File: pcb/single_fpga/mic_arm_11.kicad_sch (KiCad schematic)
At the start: 17 parts, among them U110 CDCLVC1108PW, U89 IM72D128V01XTMA1, U90 IM72D128V01XTMA1, U91 IM72D128V01XTMA1, U92 IM72D128V01XTMA1, U93 IM72D128V01XTMA1, U94 IM72D128V01XTMA1, U95 IM72D128V01XTMA1, U96 IM72D128V01XTMA1

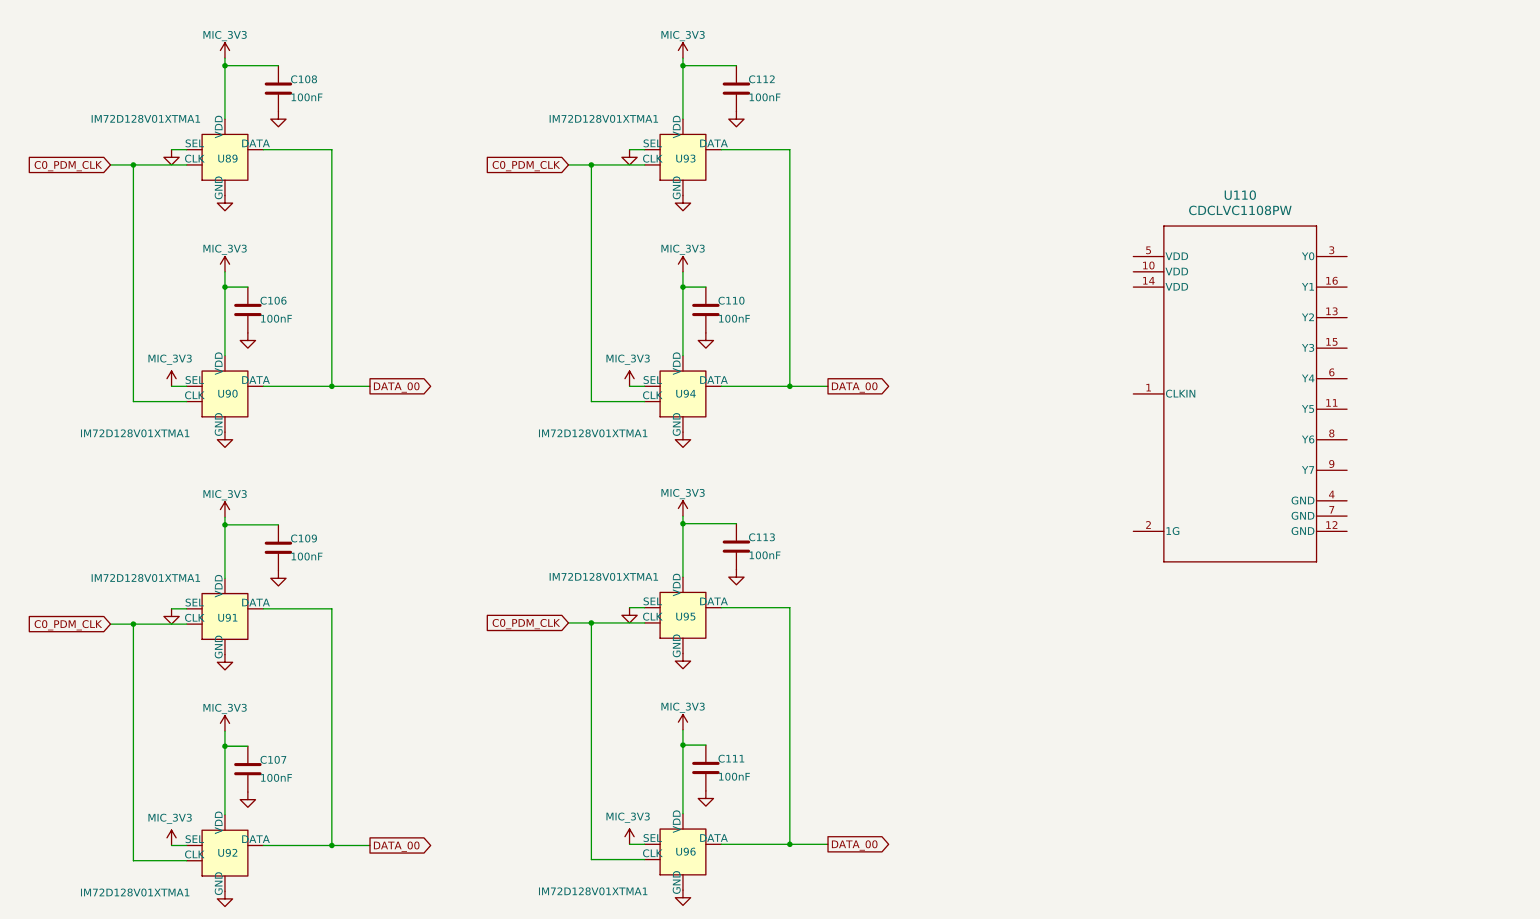
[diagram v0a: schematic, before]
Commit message: Fixed clocks and names.
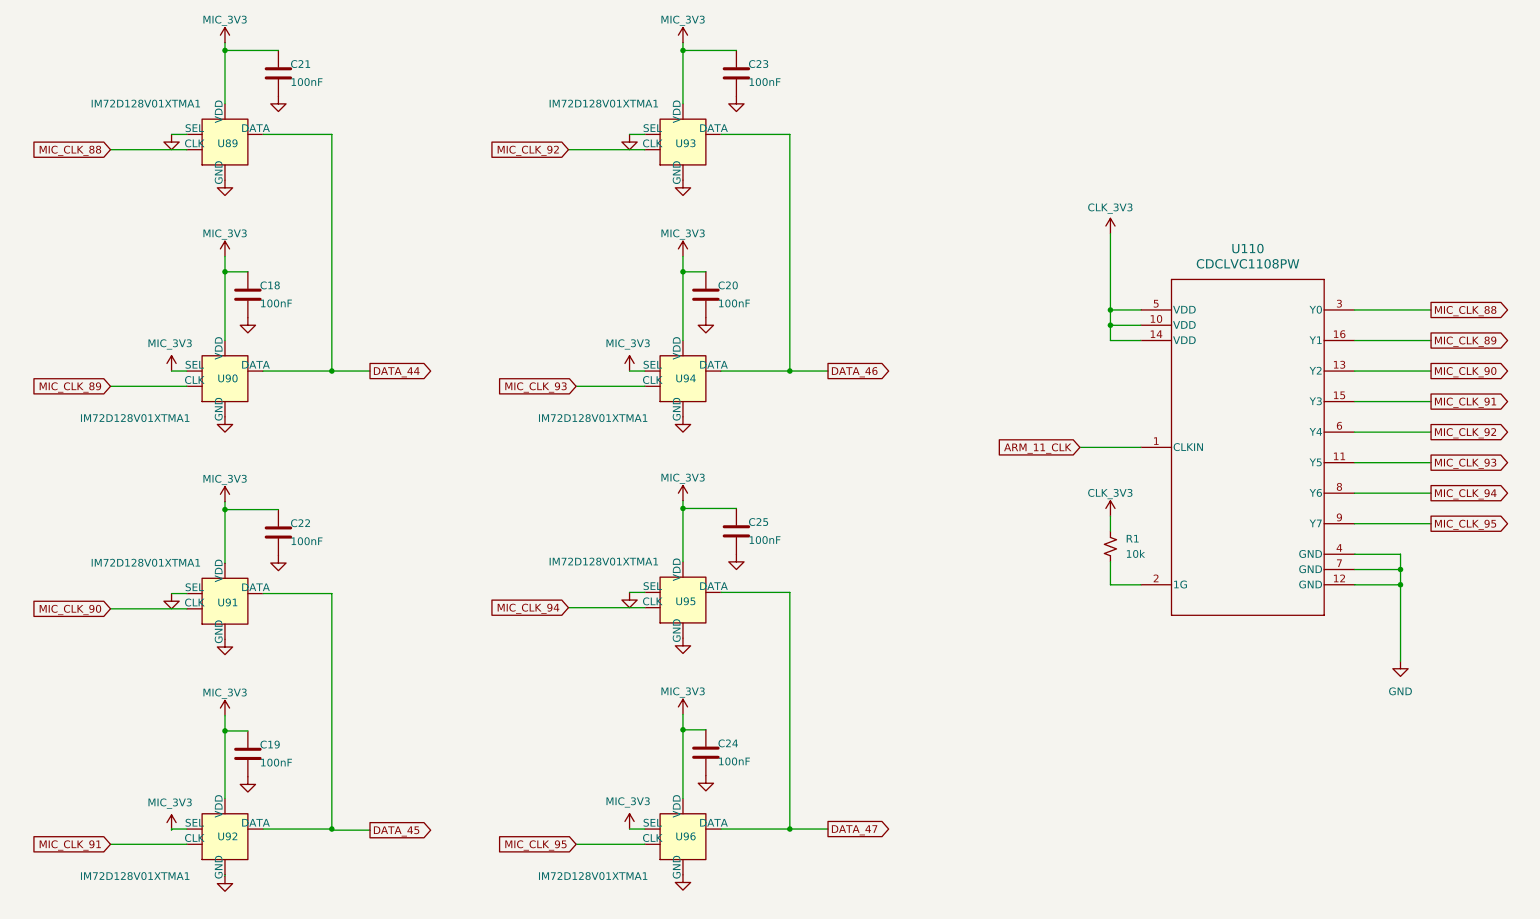
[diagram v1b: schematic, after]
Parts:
- removed C106, C107, C108, C109, C110, C111, C112, C113: 100nF, Capacitor_SMD:C_0603_1608Metric, symbol Device:C
- added C18, C19, C20, C21, C22, C23, C24, C25: 100nF, Capacitor_SMD:C_0603_1608Metric, symbol Device:C
- added R1: 10k, PCM_SparkFun-Resistor:R_0603_1608Metric, symbol PCM_SparkFun-Resistor:10k_0603
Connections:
- net GND: now also U110.12 (GND), U110.4 (GND), U110.7 (GND), C18.2, C19.2, C20.2, C21.2, C22.2, C23.2, C24.2, C25.2
- net MIC_3V3: now also C18.1, C19.1, C20.1, C21.1, C22.1, C23.1, C24.1, C25.1
- net ARM_11_CLK: now reaches U110.1 (CLKIN)
- net CLK_3V3: now reaches U110.10 (VDD)
- net CLK_3V3: now also U110.14 (VDD), U110.5 (VDD), R1.2
- net MIC_CLK_93: now reaches U110.11 (Y5)
- net MIC_CLK_93: now also U94.3 (CLK)
- net MIC_CLK_90: now reaches U110.13 (Y2)
- net MIC_CLK_90: now also U91.3 (CLK)
- net MIC_CLK_91: now reaches U110.15 (Y3)
- net MIC_CLK_91: now also U92.3 (CLK)
- net MIC_CLK_89: now reaches U110.16 (Y1)
- net MIC_CLK_89: now also U90.3 (CLK)
- net at U110.2 (1G): now also R1.1
- net MIC_CLK_88: now reaches U110.3 (Y0)
- net MIC_CLK_88: now also U89.3 (CLK)
- net MIC_CLK_92: now reaches U110.6 (Y4)
- net MIC_CLK_92: now also U93.3 (CLK)
- net MIC_CLK_94: now reaches U110.8 (Y6)
- net MIC_CLK_94: now also U95.3 (CLK)
- net MIC_CLK_95: now reaches U110.9 (Y7)
- net MIC_CLK_95: now also U96.3 (CLK)
- removed net C0_PDM_CLK: U89.3 (CLK), U90.3 (CLK), U91.3 (CLK), U92.3 (CLK), U93.3 (CLK), U94.3 (CLK), U95.3 (CLK), U96.3 (CLK)
- removed net DATA_00: U89.1 (DATA), U90.1 (DATA), U91.1 (DATA), U92.1 (DATA), U93.1 (DATA), U94.1 (DATA), U95.1 (DATA), U96.1 (DATA)
- new net DATA_44: U89.1 (DATA), U90.1 (DATA)
- new net DATA_45: U91.1 (DATA), U92.1 (DATA)
- new net DATA_46: U93.1 (DATA), U94.1 (DATA)
- new net DATA_47: U95.1 (DATA), U96.1 (DATA)

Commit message: Fixed all duplicate refdes's.
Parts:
- renumbered C18 to C106, C19 to C107, C20 to C108, C21 to C109, C22 to C110, C23 to C111, C24 to C112, C25 to C113, R1 to R16

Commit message: Fixed symbol library references.
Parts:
- U110: footprint PW0016A_N -> CDCLVC1108:PW0016A_N

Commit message: Fixed footprints. Added missing mic. Relinked placed footprints.
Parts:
- U89, U90, U91, U92, U93, U94, U95, U96: footprint (none) -> IM72D128:IFX-PG-LLGA-5-4
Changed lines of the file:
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@@
 			)
 		)
-		(property "Footprint" ""
+		(property "Footprint" "IM72D128:IFX-PG-LLGA-5-4"
 			(at 59.69 160.02 0)
 			(hide yes)
@@
 			)
 		)
-		(property "Footprint" ""
+		(property "Footprint" "IM72D128:IFX-PG-LLGA-5-4"
 			(at 135.89 160.02 0)
 			(hide yes)
@@
 			)
 		)
-		(property "Footprint" ""
+		(property "Footprint" "IM72D128:IFX-PG-LLGA-5-4"
 			(at 59.69 83.82 0)
 			(hide yes)
@@
 			)
 		)
-		(property "Footprint" ""
+		(property "Footprint" "IM72D128:IFX-PG-LLGA-5-4"
 			(at 59.69 120.65 0)
 			(hide yes)
@@
 			)
 		)
-		(property "Footprint" ""
+		(property "Footprint" "IM72D128:IFX-PG-LLGA-5-4"
 			(at 59.69 44.45 0)
 			(hide yes)
@@
 			)
 		)
-		(property "Footprint" ""
+		(property "Footprint" "IM72D128:IFX-PG-LLGA-5-4"
 			(at 135.89 83.82 0)
 			(hide yes)
@@
 			)
 		)
-		(property "Footprint" ""
+		(property "Footprint" "IM72D128:IFX-PG-LLGA-5-4"
 			(at 135.89 44.45 0)
 			(hide yes)
@@
 			)
 		)
-		(property "Footprint" ""
+		(property "Footprint" "IM72D128:IFX-PG-LLGA-5-4"
 			(at 135.89 120.65 0)
 			(hide yes)

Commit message: Updated all refdes's.
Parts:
- removed C106, C107, C108, C109, C110, C111, C112, C113: 100nF, Capacitor_SMD:C_0603_1608Metric, symbol Device:C
- removed R16: 10k, PCM_SparkFun-Resistor:R_0603_1608Metric, symbol PCM_SparkFun-Resistor:10k_0603
- removed U110: CDCLVC1108PW, CDCLVC1108:PW0016A_N, symbol CDCLVC1108:CDCLVC1108PW
- removed U89, U90, U91, U92, U93, U94, U95, U96: IM72D128V01XTMA1, IM72D128:IFX-PG-LLGA-5-4, symbol multi_fpga:IM72D128
- added C89, C90, C91, C92, C93, C94, C95, C96: 100nF, Capacitor_SMD:C_0603_1608Metric, symbol Device:C
- added R12: 10k, PCM_SparkFun-Resistor:R_0603_1608Metric, symbol PCM_SparkFun-Resistor:10k_0603
- added U100, U101, U102, U103, U104, U105, U106, U107: IM72D128V01XTMA1, IM72D128:IFX-PG-LLGA-5-4, symbol multi_fpga:IM72D128
- added U108: CDCLVC1108PW, CDCLVC1108:PW0016A_N, symbol CDCLVC1108:CDCLVC1108PW
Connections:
- net ARM_11_CLK: now also U108.1 (CLKIN)
- net CLK_3V3: now also R12.2, U108.10 (VDD), U108.14 (VDD), U108.5 (VDD)
- net DATA_44: now also U100.1 (DATA), U101.1 (DATA)
- net DATA_45: now also U102.1 (DATA), U103.1 (DATA)
- net DATA_46: now also U104.1 (DATA), U105.1 (DATA)
- net DATA_47: now also U106.1 (DATA), U107.1 (DATA)
- net GND: now also C89.2, C90.2, C91.2, C92.2, C93.2, C94.2, C95.2, C96.2, U100.4 (SEL), U100.5 (GND), U101.5 (GND), U102.4 (SEL), U102.5 (GND), U103.5 (GND), U104.4 (SEL), U104.5 (GND), U105.5 (GND), U106.4 (SEL), U106.5 (GND), U107.5 (GND), U108.12 (GND), U108.4 (GND), U108.7 (GND)
- net MIC_3V3: now also C89.1, C90.1, C91.1, C92.1, C93.1, C94.1, C95.1, C96.1, U100.2 (VDD), U101.2 (VDD), U101.4 (SEL), U102.2 (VDD), U103.2 (VDD), U103.4 (SEL), U104.2 (VDD), U105.2 (VDD), U105.4 (SEL), U106.2 (VDD), U107.2 (VDD), U107.4 (SEL)
- net MIC_CLK_88: now also U100.3 (CLK), U108.3 (Y0)
- net MIC_CLK_89: now also U101.3 (CLK), U108.16 (Y1)
- net MIC_CLK_90: now also U102.3 (CLK), U108.13 (Y2)
- net MIC_CLK_91: now also U103.3 (CLK), U108.15 (Y3)
- net MIC_CLK_92: now also U104.3 (CLK), U108.6 (Y4)
- net MIC_CLK_93: now also U105.3 (CLK), U108.11 (Y5)
- net MIC_CLK_94: now also U106.3 (CLK), U108.8 (Y6)
- net MIC_CLK_95: now also U107.3 (CLK), U108.9 (Y7)
- new net: R12.1, U108.2 (1G)
